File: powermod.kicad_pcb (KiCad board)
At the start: 4 copper layers, 27 x 18 mm, 21 parts, among them J1 Conn_02x07_Odd_Even, J2 Conn_02x07_Odd_Even, U1 TPS54260DGQ

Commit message: feat: reduced crosstalk between sw and comp
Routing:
- net /SW: track 22.1 -> 22.9 mm
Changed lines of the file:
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@@
-	)
-	(segment
-		(start 31.029999 46)
-		(end 35 46)
-		(width 0.3)
-		(layer "In1.Cu")
-		(net 4)
 	)
 	(segment
@@
 		(net 4)
 	)
+	(segment
+		(start 33.779999 45.720001)
+		(end 35 44.5)
+		(width 0.3)
+		(layer "B.Cu")
+		(net 4)
+	)
+	(segment
+		(start 30.75 45.720001)
+		(end 33.779999 45.720001)
+		(width 0.3)
+		(layer "B.Cu")
+		(net 4)
+	)

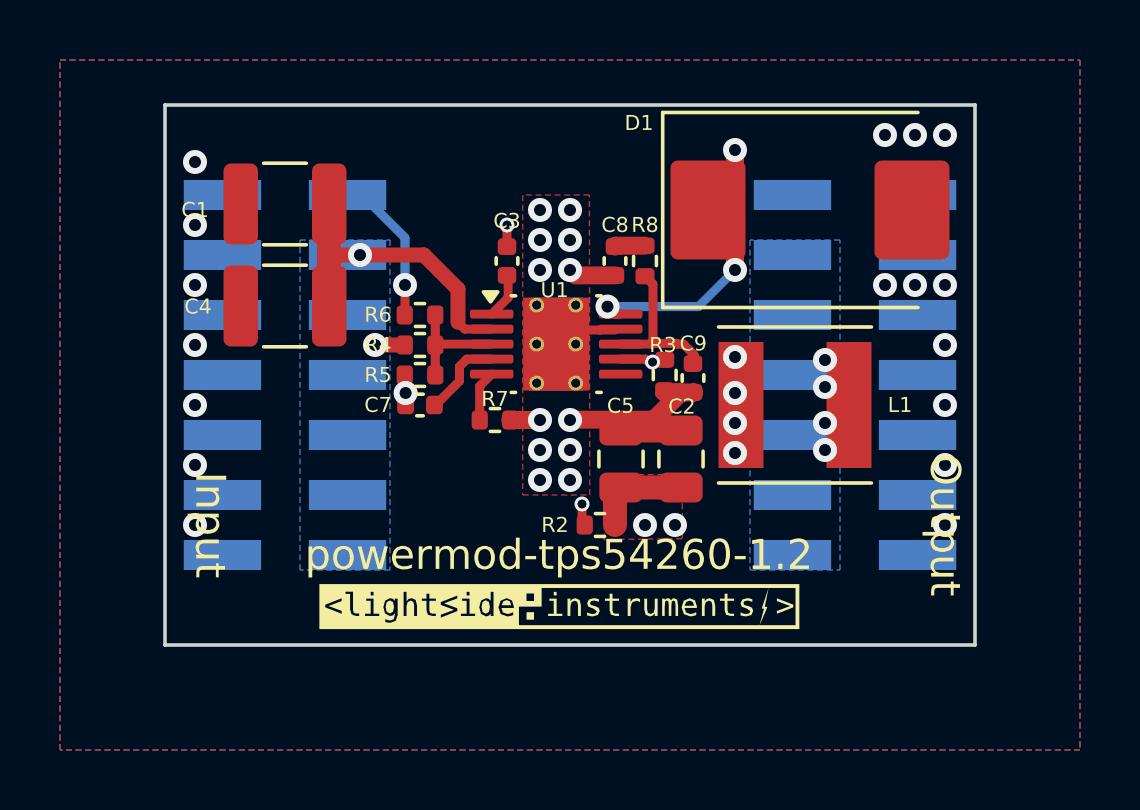
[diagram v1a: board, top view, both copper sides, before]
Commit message: feat: reduced crosstalk between sw and +5v
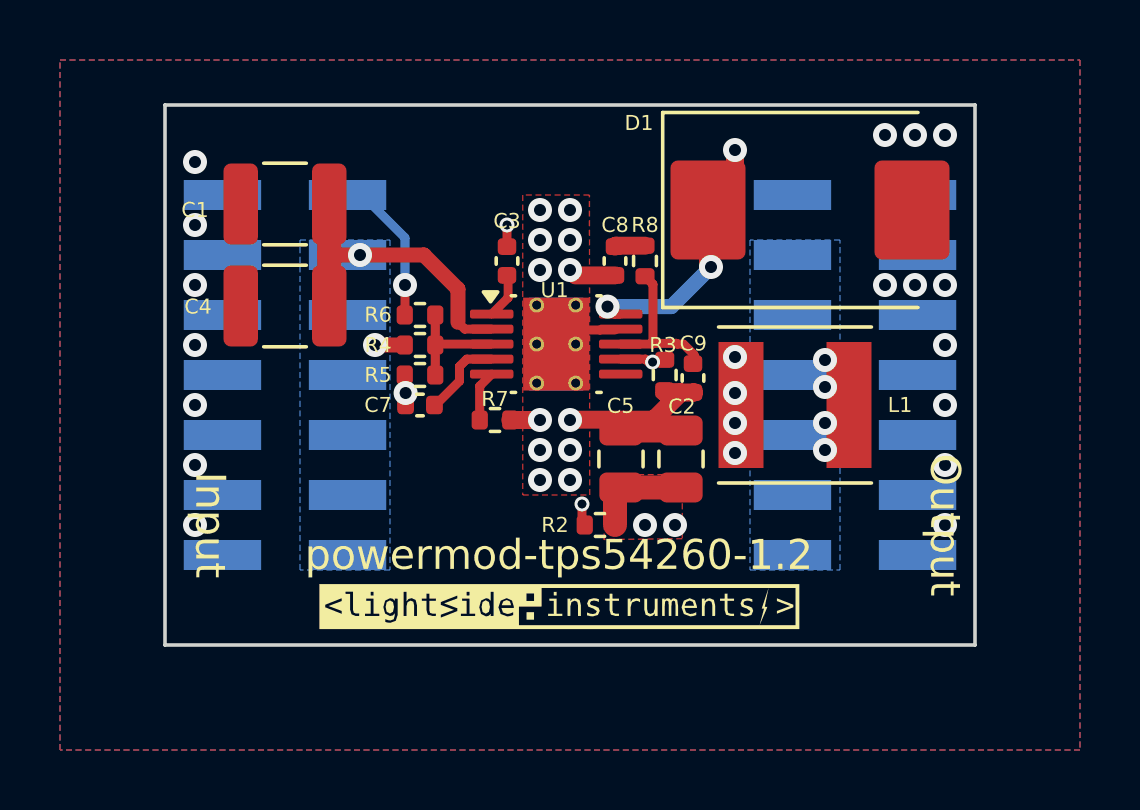
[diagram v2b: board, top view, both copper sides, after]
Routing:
- net /SW: track 22.9 -> 21.7 mm
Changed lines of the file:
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@@
-	)
-	(segment
-		(start 35 43.4)
-		(end 34.1 42.5)
-		(width 0.6)
-		(layer "F.Cu")
-		(net 4)
 	)
 	(segment
@@
 		(end 34.1 42.5)
 		(width 0.25)
+		(layer "F.Cu")
+		(net 4)
+	)
+	(segment
+		(start 34.2 44.4)
+		(end 34.1 44.3)
+		(width 0.6)
 		(layer "F.Cu")
 		(net 4)
@@
 	)
 	(segment
-		(start 35 44.5)
-		(end 35 43.4)
+		(start 34.1 44.3)
+		(end 34.1 42.5)
 		(width 0.6)
 		(layer "F.Cu")
@@
 	)
 	(via
-		(at 35 44.5)
+		(at 34.2 44.4)
 		(size 0.8)
 		(drill 0.4)
@@
 	)
 	(segment
-		(start 33.779999 45.720001)
-		(end 35 44.5)
-		(width 0.3)
+		(start 32.879999 45.720001)
+		(end 30.75 45.720001)
+		(width 0.5)
 		(layer "B.Cu")
 		(net 4)
 	)
 	(segment
-		(start 30.75 45.720001)
-		(end 33.779999 45.720001)
-		(width 0.3)
+		(start 34.2 44.4)
+		(end 32.879999 45.720001)
+		(width 0.5)
 		(layer "B.Cu")
 		(net 4)
